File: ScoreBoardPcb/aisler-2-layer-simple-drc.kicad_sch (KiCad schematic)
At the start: 16 parts, among them J1 Conn_02x20_Odd_Even, U1 CD4066BM96, U2 CD4066BM96, U3 CD4066BM96, U4 CD4066BM96, U5 ADM3101EARQZ-REEL

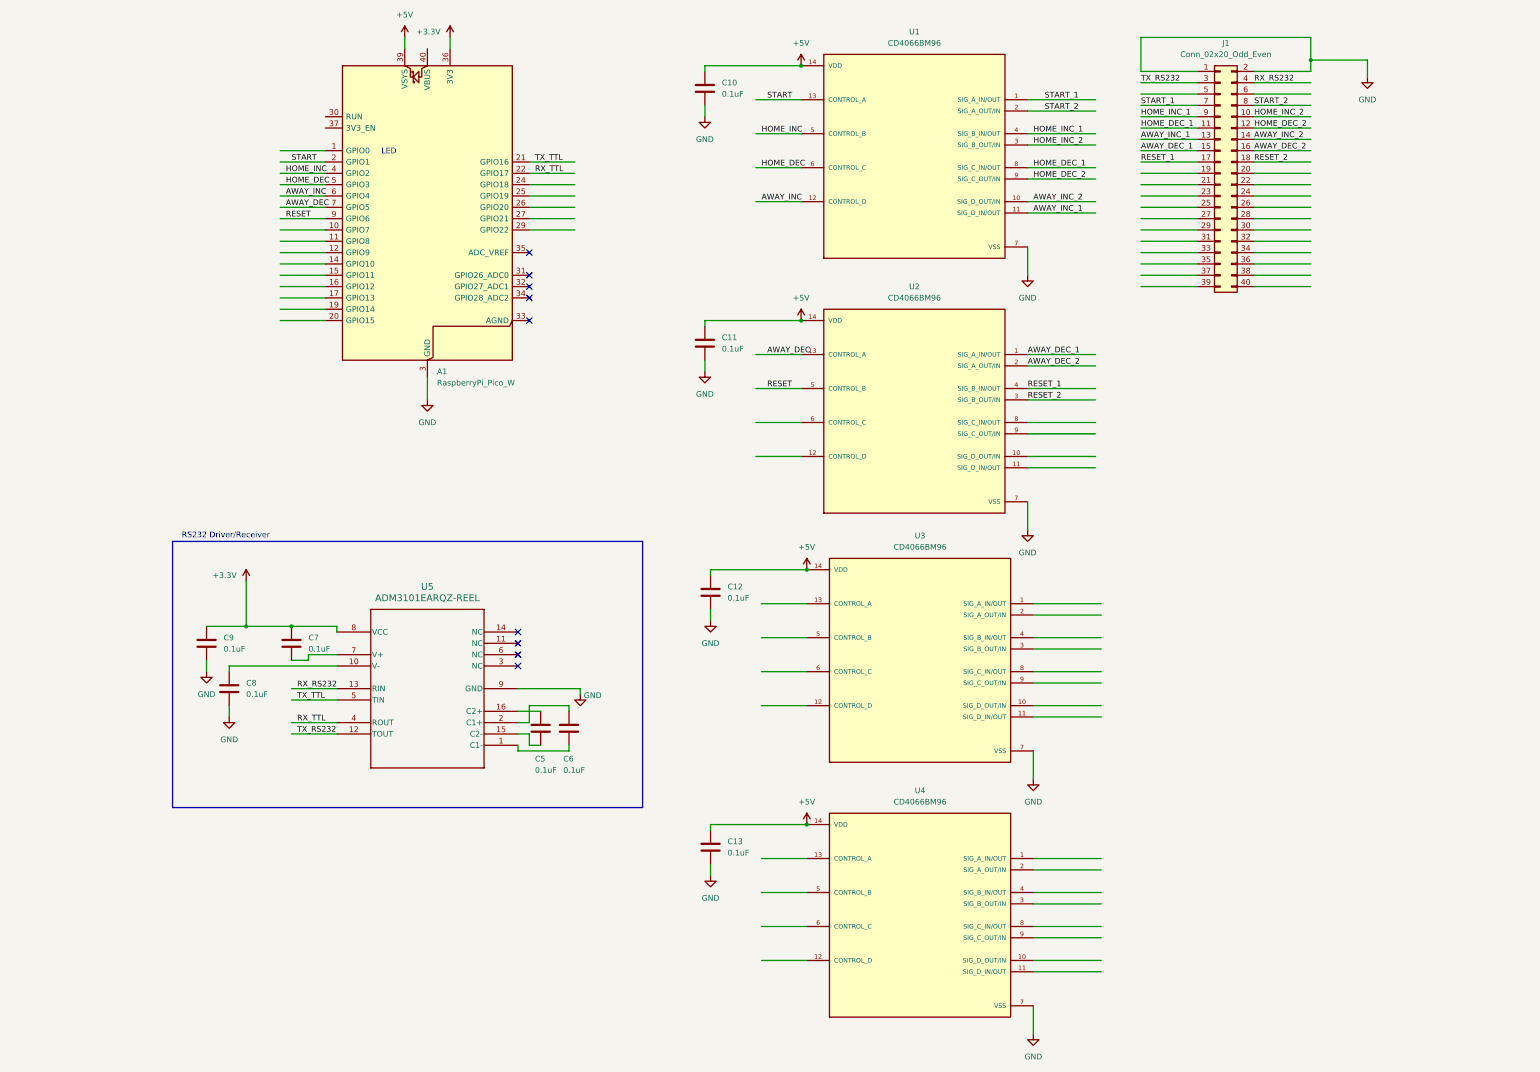
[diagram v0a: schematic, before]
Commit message: Routed with mounting holes
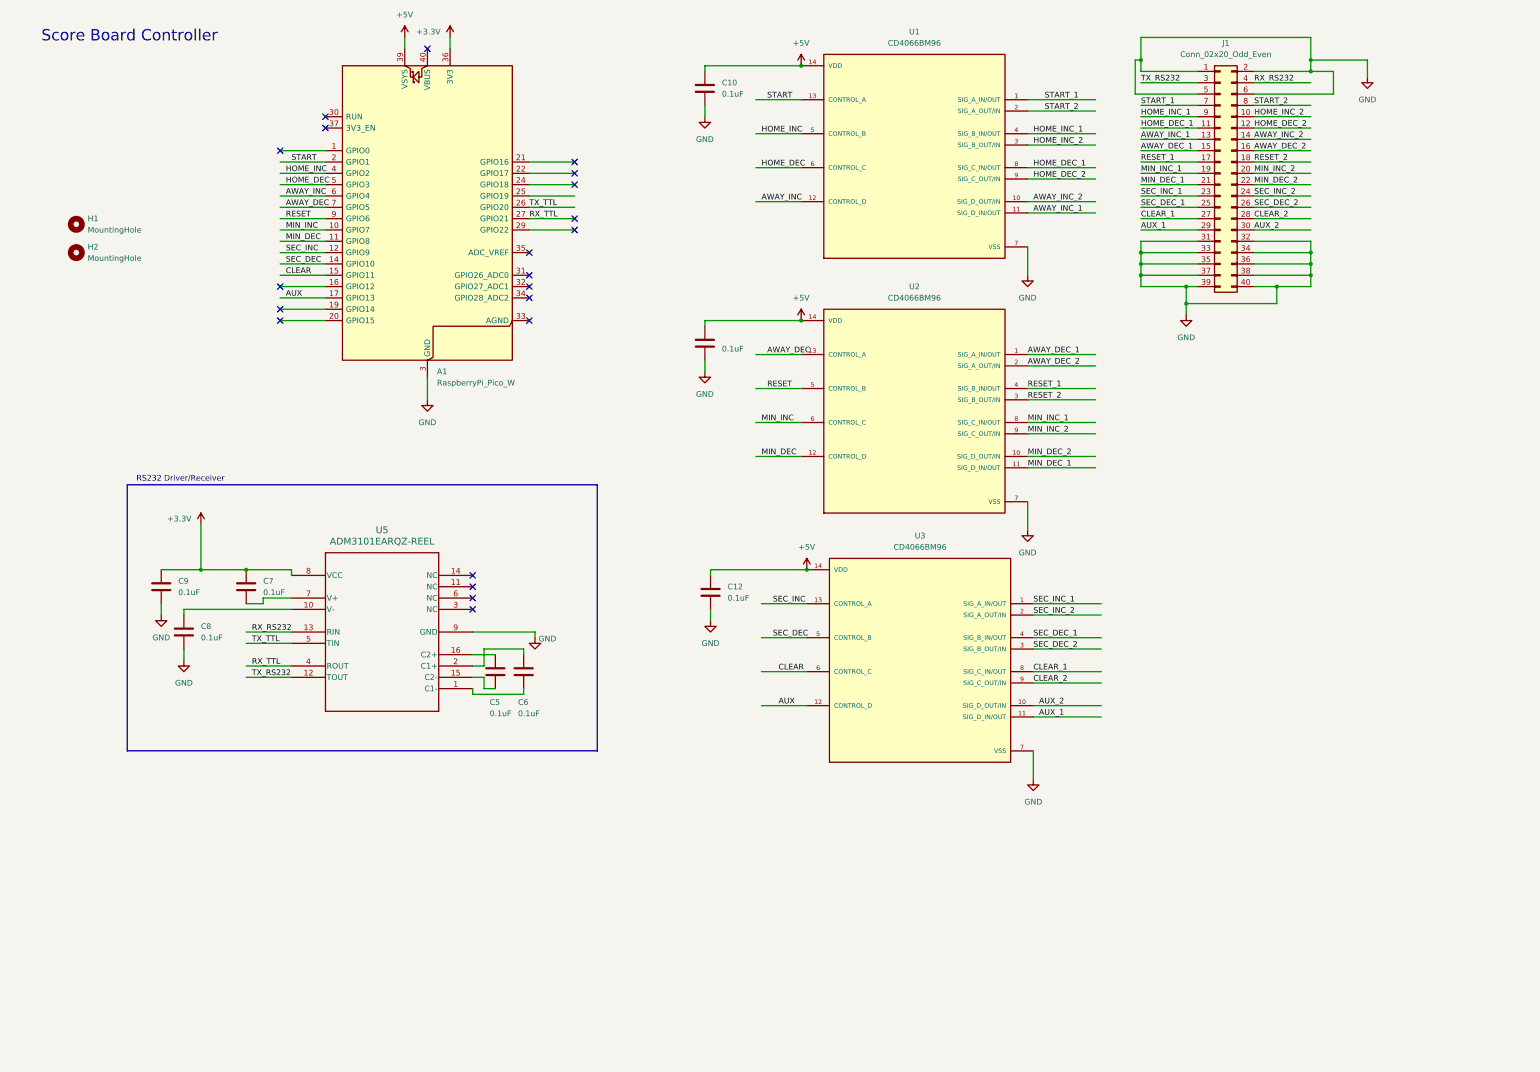
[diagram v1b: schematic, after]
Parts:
- removed C11: 0.1uF, Capacitor_SMD:C_0402_1005Metric_Pad0.74x0.62mm_HandSolder, symbol Device:C
- removed U4: CD4066BM96, ScoreBoardPcb:SOIC127P600X175-14N, symbol CD4066BM96:CD4066BM96
- added H1, H2: MountingHole, MountingHole:MountingHole_3.2mm_M3, symbol Mechanical:MountingHole
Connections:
- net GND: now also J1.31 (Pin_31), J1.32 (Pin_32), J1.33 (Pin_33), J1.34 (Pin_34), J1.35 (Pin_35), J1.36 (Pin_36), J1.37 (Pin_37), J1.38 (Pin_38), J1.39 (Pin_39), J1.40 (Pin_40), J1.5 (Pin_5), J1.6 (Pin_6)
- net RX_TTL: now also A1.27 (GPIO21); no longer A1.22 (GPIO17)
- net TX_TTL: now also A1.26 (GPIO20); no longer A1.21 (GPIO16)
- net MIN_INC_1: now reaches J1.19 (Pin_19)
- net MIN_INC_1: now also U2.8 (SIG_C_IN/OUT)
- net MIN_INC_2: now reaches J1.20 (Pin_20)
- net MIN_INC_2: now also U2.9 (SIG_C_OUT/IN)
- net MIN_DEC_1: now reaches J1.21 (Pin_21)
- net MIN_DEC_1: now also U2.11 (SIG_D_IN/OUT)
- net MIN_DEC_2: now reaches J1.22 (Pin_22)
- net MIN_DEC_2: now also U2.10 (SIG_D_OUT/IN)
- net SEC_INC_1: now reaches J1.23 (Pin_23)
- net SEC_INC_1: now also U3.1 (SIG_A_IN/OUT)
- net SEC_INC_2: now reaches J1.24 (Pin_24)
- net SEC_INC_2: now also U3.2 (SIG_A_OUT/IN)
- net SEC_DEC_1: now reaches J1.25 (Pin_25)
- net SEC_DEC_1: now also U3.4 (SIG_B_IN/OUT)
- net SEC_DEC_2: now reaches J1.26 (Pin_26)
- net SEC_DEC_2: now also U3.3 (SIG_B_OUT/IN)
- net CLEAR_1: now reaches J1.27 (Pin_27)
- net CLEAR_1: now also U3.8 (SIG_C_IN/OUT)
- net CLEAR_2: now reaches J1.28 (Pin_28)
- net CLEAR_2: now also U3.9 (SIG_C_OUT/IN)
- net AUX_1: now reaches J1.29 (Pin_29)
- net AUX_1: now also U3.11 (SIG_D_IN/OUT)
- net AUX_2: now reaches J1.30 (Pin_30)
- net AUX_2: now also U3.10 (SIG_D_OUT/IN)
- net MIN_INC: now reaches A1.10 (GPIO7)
- net MIN_INC: now also U2.6 (CONTROL_C)
- net MIN_DEC: now reaches A1.11 (GPIO8)
- net MIN_DEC: now also U2.12 (CONTROL_D)
- net SEC_INC: now reaches A1.12 (GPIO9)
- net SEC_INC: now also U3.13 (CONTROL_A)
- net SEC_DEC: now reaches A1.14 (GPIO10)
- net SEC_DEC: now also U3.5 (CONTROL_B)
- net CLEAR: now reaches A1.15 (GPIO11)
- net CLEAR: now also U3.6 (CONTROL_C)
- net AUX: now reaches A1.17 (GPIO13)
- net AUX: now also U3.12 (CONTROL_D)
- no-connect marks 9 -> 21
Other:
- note added: "Score Board Controller"
- note removed: "LED"
- moved on the sheet: C5, C6, C7, C8, C9, U5

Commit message: Update to use CD74HCT4066M96
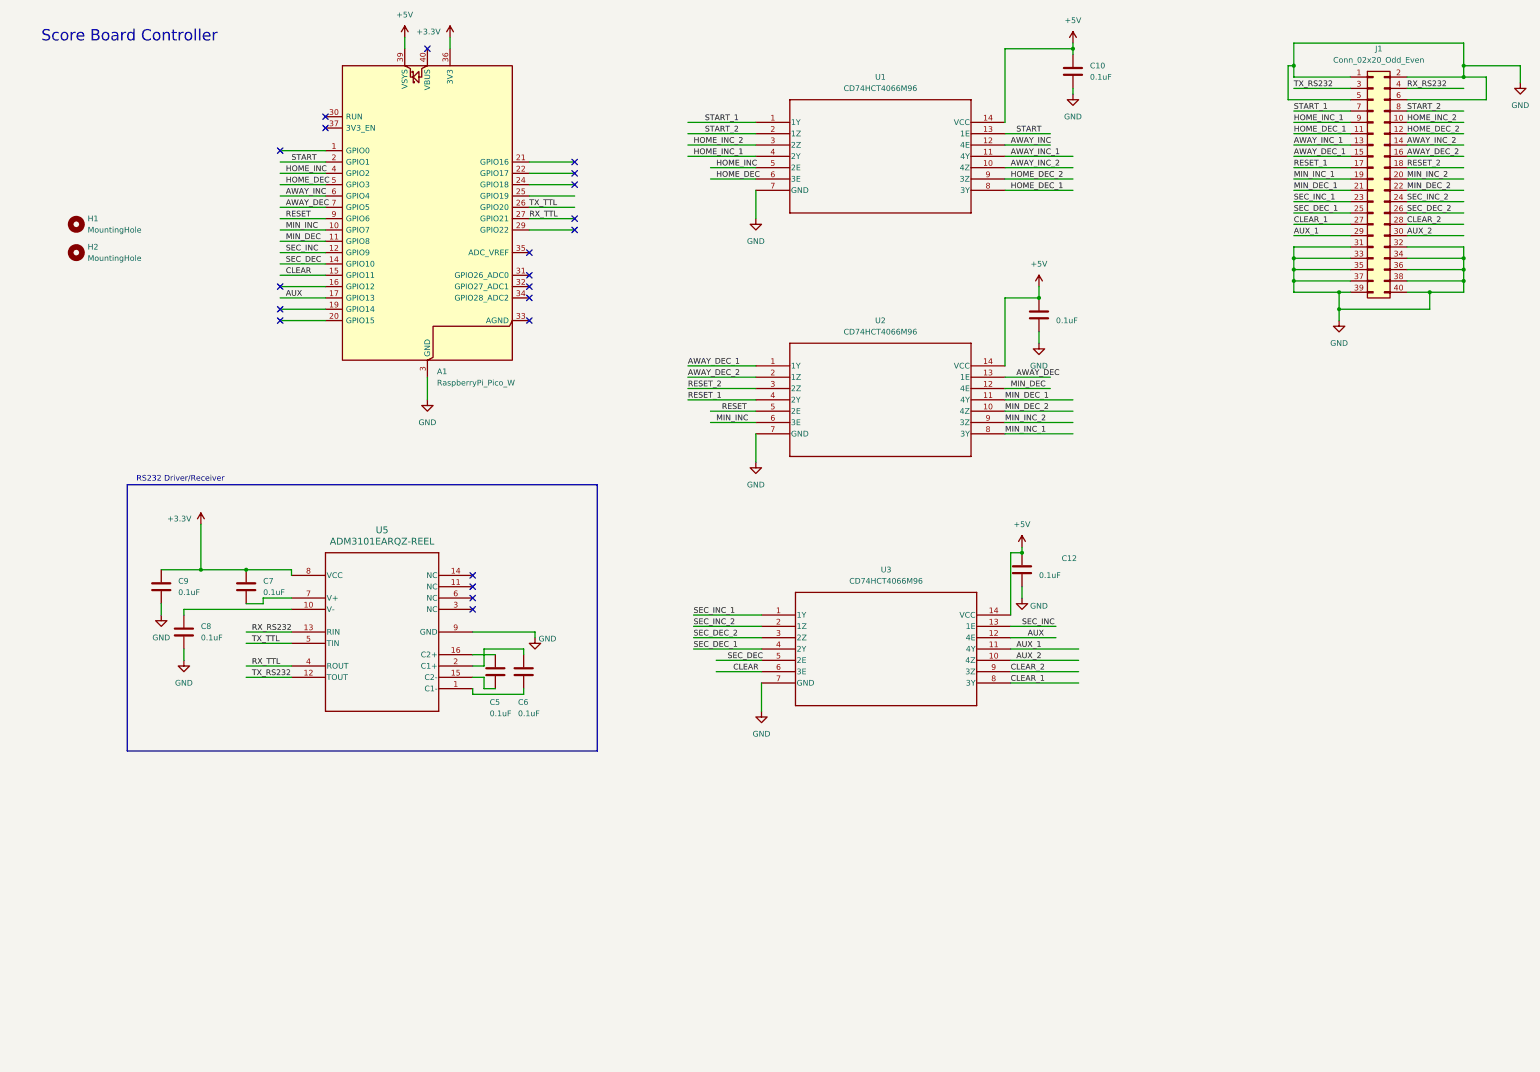
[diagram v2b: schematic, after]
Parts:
- U1, U2, U3: value CD4066BM96 -> CD74HCT4066M96; footprint ScoreBoardPcb:SOIC127P600X175-14N -> ScoreBoardPcb:D14-M; symbol CD4066BM96:CD4066BM96 -> CD74HCT4066M96:CD74HCT4066M96
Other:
- moved on the sheet: C10, C12, J1

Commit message: Rev 1.0 submitted for manf
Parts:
- A1: footprint Module:RaspberryPi_Pico_Common_THT -> ScoreBoardPcb:RaspberryPi_Pico_Common_THT
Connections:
- net +5V: now also J1.2 (Pin_2); no longer A1.39 (VSYS)
- net GND: no longer J1.2 (Pin_2)
